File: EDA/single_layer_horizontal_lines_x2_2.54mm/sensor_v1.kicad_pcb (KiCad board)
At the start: 2 copper layers, 54 x 58 mm, 2 parts

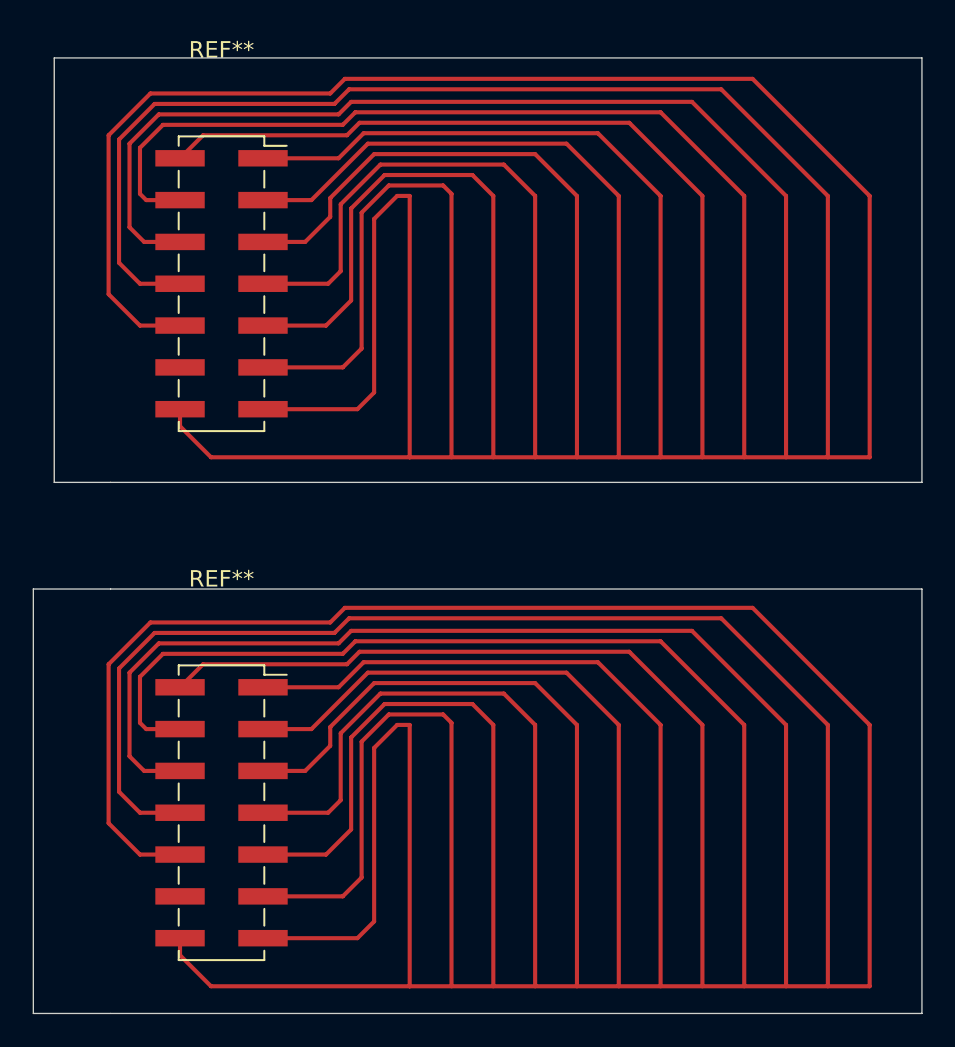
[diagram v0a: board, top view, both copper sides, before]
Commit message: add flare on trace connections to 5V rail
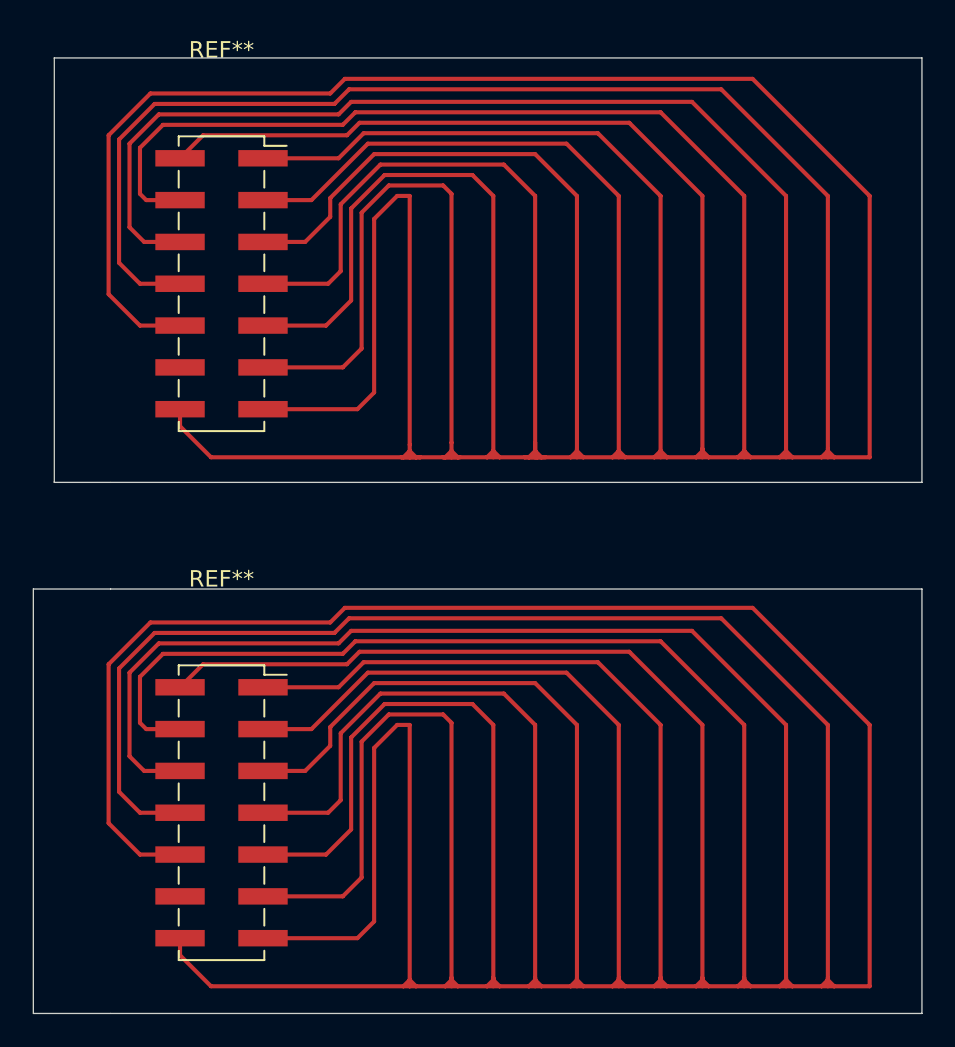
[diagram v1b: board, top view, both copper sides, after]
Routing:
- net (no net): track 1298.6 -> 1328.2 mm
